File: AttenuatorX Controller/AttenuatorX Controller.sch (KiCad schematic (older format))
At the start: 3 parts

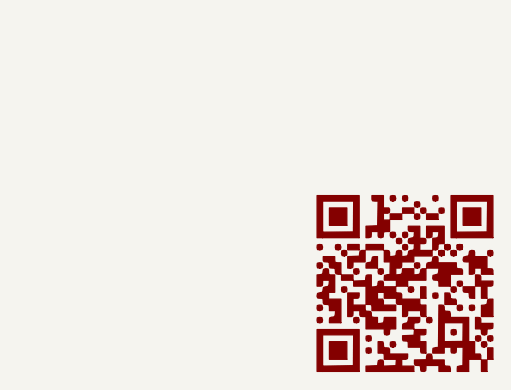
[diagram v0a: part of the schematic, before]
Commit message: Updated BOM and Libraries
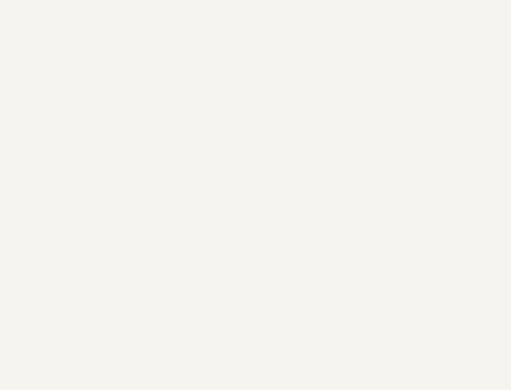
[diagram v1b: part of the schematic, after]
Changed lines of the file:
@@
-EESchema Schematic File Version 2  date 11/9/2011 9:58:21 PM
+EESchema Schematic File Version 2  date 11/30/2011 4:39:06 PM
 LIBS:power
 LIBS:device
@@
 LIBS:valves
 LIBS:AttenuatorX
-LIBS:PASLogo
 LIBS:AttenuatorX Controller-cache
 EELAYER 25  0
@@
 Sheet 1 1
 Title ""
-Date "8 nov 2011"
+Date "30 nov 2011"
 Rev ""
 Comp ""
@@
 Comment4 ""
 $EndDescr
-$Comp
-L LOGO #G?
-U 1 1 4EB95E35
-P 11850 10050
-F 0 "#G?" H 11850 9670 80  0001 C CNN
-F 1 "LOGO" H 11850 10430 60  0001 C CNN
-	1    11850 10050
-	1    0    0    -1
-$EndComp
 Text Label 3200 1850 0    60   ~ 0
 VCC

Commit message: Updated BOM, Controller, and Libraries
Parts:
- added U?: ATMEGA168A, symbol ATMEGA168A
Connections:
- wire segments 11 -> 8
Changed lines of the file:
@@
-EESchema Schematic File Version 2  date 11/30/2011 4:39:06 PM
+EESchema Schematic File Version 2  date 12/1/2011 10:25:59 PM
 LIBS:power
 LIBS:device
@@
 Sheet 1 1
 Title ""
-Date "30 nov 2011"
+Date "1 dec 2011"
 Rev ""
 Comp ""
@@
 Comment4 ""
 $EndDescr
-Text Label 3200 1850 0    60   ~ 0
-VCC
-Connection ~ 3000 1850
+Wire Notes Line
+	3500 1500 1300 1500
+Wire Notes Line
+	3500 1500 3500 2900
+Wire Notes Line
+	3500 2900 1300 2900
+Wire Notes Line
+	1300 2900 1300 1500
+Connection ~ 1550 1850
 Wire Wire Line
-	3350 1850 3000 1850
+	1550 2300 1550 1700
 Wire Wire Line
-	3000 1850 2800 1850
+	3000 1900 3000 1850
+Connection ~ 1550 2250
+Wire Wire Line
+	1550 2250 1700 2250
+Wire Wire Line
+	1550 1850 1700 1850
+Wire Wire Line
+	1700 2050 1700 2100
+Wire Wire Line
+	1550 2700 1550 2750
 Wire Wire Line
 	3000 2300 3000 2350
 Wire Wire Line
-	1550 2700 1550 2750
-Wire Wire Line
-	1700 2050 1700 2100
-Wire Wire Line
-	1550 1850 1700 1850
-Wire Wire Line
-	1550 2250 1700 2250
-Connection ~ 1550 2250
-Wire Wire Line
-	3000 1850 3000 1900
-Wire Wire Line
-	1550 1700 1550 1850
-Wire Wire Line
-	1550 1850 1550 2250
-Wire Wire Line
-	1550 2250 1550 2300
-Connection ~ 1550 1850
+	2800 1850 3350 1850
+Connection ~ 3000 1850
+$Comp
+L ATMEGA168A U?
+U 1 1 4ED7BF31
+P 8200 5150
+F 0 "U?" H 9200 4050 60  0000 C CNN
+F 1 "ATMEGA168A" H 8200 6150 60  0000 C CNN
+	1    8200 5150
+	1    0    0    -1
+$EndComp
+Text Label 3200 1850 0    60   ~ 0
+VCC
 $Comp
 L +5V #PWR?
